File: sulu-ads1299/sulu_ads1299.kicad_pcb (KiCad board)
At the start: 2 copper layers, 42.7 x 64.6 mm, 82 parts, among them J1 73391-0060, J10 through_hole, J11 through_hole, J12 through_hole, J13 through_hole, J14 through_hole, J15 through_hole, J16 through_hole, J17 through_hole, J18 through_hole, J19 through_hole, J2 Conn_01x02, J20 through_hole, J21 through_hole, J22 through_hole, J23 through_hole, J24 through_hole, J25 through_hole, J3 Conn_01x10, J4 Conn_02x10_Odd_Even, J5 Conn_02x11_Odd_Even, J6 Conn_01x02, J7 Conn_02x07_Odd_Even, J8 through_hole, J9 through_hole, SW1 SW_Push, U1 S-85S1AB18-I6T1U, U2 S-85S1AB11-I6T1U, U3 LM2775DSG, U4 ADS1299_TQFP-64, U5 scum3

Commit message: Sulu-ADS1299 started revision 2, added Molex libs, Banana for scale
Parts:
- removed J4: Conn_02x10_Odd_Even, Connector_PinSocket_2.54mm:PinSocket_2x10_P2.54mm_Vertical
- removed J5: Conn_02x11_Odd_Even, Connector_PinSocket_2.54mm:PinSocket_2x11_P2.54mm_Vertical
- removed J7: Conn_02x07_Odd_Even, Connector_PinHeader_2.54mm:PinHeader_2x07_P2.54mm_Vertical
- removed R15: 0 Ohm, Resistor_SMD:R_0402_1005Metric
- removed R3: 42.2K, Resistor_SMD:R_0402_1005Metric
- removed R4: 66.5K, Resistor_SMD:R_0402_1005Metric
- added G***: LOGO, Banana:Banana, F.Cu at (69.8, 54.4)
- added TP1: TestPoint, SCUM:through_hole, F.Cu at (151.3, 72.5)
- added TP10: TestPoint, SCUM:through_hole, F.Cu at (165.6, 59.7)
- added TP11: TestPoint, SCUM:through_hole, F.Cu at (153.1, 72.5)
- added TP12: TestPoint, SCUM:through_hole, F.Cu at (150.8, 74.4)
- added TP13: TestPoint, SCUM:through_hole, F.Cu at (145.0, 80.0)
- added TP14: TestPoint, SCUM:through_hole, F.Cu at (154.3, 69.8)
- added TP15: TestPoint, SCUM:through_hole, F.Cu at (146.2, 74.1)
- added TP16: TestPoint, SCUM:through_hole, F.Cu at (143.3, 80.0)
- added TP2: TestPoint, SCUM:through_hole, F.Cu at (158.6, 66.1)
- added TP3: TestPoint, SCUM:through_hole, F.Cu at (146.2, 78.0)
- added TP4: TestPoint, SCUM:through_hole, F.Cu at (163.8, 59.7)
- added TP5: TestPoint, SCUM:through_hole, F.Cu at (163.3, 61.7)
- added TP6: TestPoint, SCUM:through_hole, F.Cu at (149.1, 76.2)
- added TP7: TestPoint, SCUM:through_hole, F.Cu at (149.1, 74.4)
- added TP8: TestPoint, SCUM:through_hole, F.Cu at (166.8, 57.7)
- added TP9: TestPoint, SCUM:through_hole, F.Cu at (155.7, 68.1)
- C6: value 2.2 uF -> 10 uF
- C_1.8_IN1: value 10 uF -> 4.7 uF
- C_1.8_OUT1: value 10 uF -> 22 uF
- J2: value Conn_01x02 -> Conn_02x05_Odd_Even; footprint Connector_PinHeader_2.54mm:PinHeader_1x02_P2.54mm_Vertical -> Connector_PinSocket_2.54mm:PinSocket_2x05_P2.54mm_Vertical_SMD
- J3: value Conn_01x10 -> Conn_01x08; footprint Connector_PinSocket_2.54mm:PinSocket_1x10_P2.54mm_Vertical -> Molex Connectors:Molex_PicoBlade_53047-0810_1x08_P1.25mm_Vertical; moved to F.Cu
- L1: value 2.2 uH -> 4.7 uH
- SW1: value SW_Push -> SW_DIP_x02; footprint Button_Switch_THT:SW_PUSH_6mm -> Button_Switch_SMD:SW_DIP_SPSTx02_Slide_6.7x6.64mm_W6.73mm_P2.54mm_LowProfile_JPin
- U1: value S-85S1AB18-I6T1U -> TPS62222DDCT; footprint downloaded_libs:SOFL50P180X50-6N -> Package_TO_SOT_SMD:SOT-23-5
- moved J24 110.1 mm to (194.1, 55.8)
- moved J16 108.0 mm to (192.9, 57.7)
- moved J25 107.9 mm to (194.7, 57.5)
- moved C18 105.5 mm to (188.8, 85.6), turned to 0 degrees
- moved C8 105.5 mm to (188.8, 79.7), turned to 0 degrees
- moved C25 105.1 mm to (188.8, 57.9), turned to 0 degrees
- moved J13 103.2 mm to (191.8, 59.5)
- moved C10 101.3 mm to (191.7, 81.7), turned to 0 degrees
- moved C17 98.1 mm to (181.8, 92.1), turned to 0 degrees
- moved J11 98.1 mm to (191.8, 61.3)
- moved J9 97.1 mm to (188.3, 59.7)
- moved J14 96.8 mm to (183.2, 70.1)
- moved J8 95.9 mm to (194.0, 77.6)
- moved J23 95.5 mm to (181.5, 70.1)
- moved C9 92.6 mm to (178.9, 94.0), turned to 0 degrees
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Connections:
- C10 pad 1: /SCUM_GPIO7 -> +1.8V_REG
- C11 pad 1: /SCUM_GPIO7 -> +1.8V_REG
- C21 pad 1: +VDDD -> +1.1V_REG
- C22 pad 1: +VDDD -> +1.1V_REG
- J2 pad 1: /~{ADS_PWDN} -> /ADS_IN1P_CONN
- J2 pad 2: GND -> /ADS_IN1N_CONN
- J3 pad 2: +NRF_VDDD -> /HARD_RESET
- J3 pad 3: +NRF_GND -> /3WB_DATA
- J3 pad 4: /HARD_RESET -> /3WB_ENB
- J3 pad 5: /3WB_DATA -> /3WB_CLK
- J3 pad 6: /3WB_ENB -> /RsRx
- J3 pad 7: GND -> /RsTx
- J3 pad 8: /3WB_CLK -> GND
- R1 pad 1: /SCUM_GPIO7 -> +1.8V_REG
- R2 pad 1: /SCUM_GPIO7 -> +1.8V_REG
- R5 pad 1: +VDDD -> +1.1V_REG
- SW1 pad 2: GND -> /~{ADS_PWDN}
- U1 pad 1: +1.8V_REG -> +EXT_BAT
- U1 pad 3: Net-(L1-Pad2) -> +EXT_BAT
- U1 pad 4: GND -> +1.8V_REG
- U1 pad 5: +EXT_BAT -> Net-(L1-Pad2)
- U4 pad 48: /SCUM_GPIO7 -> +1.8V_REG
- U4 pad 50: /SCUM_GPIO7 -> +1.8V_REG
- U4 pad 52: /SCUM_GPIO7 -> +1.8V_REG
- U5 pad 36: +VDDIO -> +1.8V_REG
- U5 pad 4: +VBAT -> +1.8V_REG
- U5 pad 61: /BOOT_SOURCE_SEL -> +1.1V_REG
- U5 pad 62: +VBAT -> +1.8V_REG
- U5 pad 72: +VDDD -> +1.1V_REG
- U5 pad 90: +VDDD -> +1.1V_REG
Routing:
- net +EXT_BAT: track 82.7 -> 0.00 mm, vias 4 -> 0
- net +5V_REG: track 79.1 -> 0.00 mm, vias 4 -> 0
- net /SCUM_GPIO7: track 59.4 -> 0.00 mm, vias 1 -> 0
- net +VBAT: track 58.1 -> 0.00 mm, vias 2 -> 0
- net +VDDIO: track 45.7 -> 0.00 mm, vias 2 -> 0
- net GND: track 44.6 -> 0.00 mm, vias 1 -> 0
- net /~{ADS_RESET}: track 38.8 -> 0.00 mm
- net +VDDD: track 38.0 -> 0.00 mm
- net /ADS_GPIO3: track 35.2 -> 0.00 mm, vias 1 -> 0
- net /ADS_GPIO4: track 34.0 -> 0.00 mm, vias 1 -> 0
- net /ADS_GPIO1: track 30.7 -> 0.00 mm, vias 1 -> 0
- net /ADS_GPIO2: track 29.9 -> 0.00 mm, vias 1 -> 0
- net /SENSOR_LDO_OUTPUT: track 26.9 -> 0.00 mm, vias 1 -> 0
- net /SCUM_GPIO14: track 21.8 -> 0.00 mm, vias 1 -> 0
- net /BOOT_SOURCE_SEL: track 21.4 -> 0.00 mm, vias 1 -> 0
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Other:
- board size 42.7 x 64.6 mm -> 42.7 x 35.4 mm
- board text removed: "+"
- board text removed: "-"
- board text removed: "0"
- board text removed: "1"
- board text removed: "10"
- board text removed: "11"
- board text removed: "12"
- board text removed: "13"
- board text removed: "14"
- board text removed: "15"
- board text removed: "2"
- board text removed: "3"
- board text removed: "3WB CLK"
- board text removed: "3WB DATA"
- board text removed: "3WB ENB"
- board text removed: "4"
- board text removed: "5"
- board text removed: "6"
- board text removed: "7"
- board text removed: "8"
- board text removed: "9"
- board text removed: "ADC IN"
- board text removed: "ADS_PWDN"
- board text removed: "ADS_RESET"
- board text removed: "GPIO"
- board text removed: "GPIO1"
- board text removed: "GPIO2"
- board text removed: "GPIO3"
- board text removed: "GPIO4"
- board text removed: "HARD RESET"
- board text removed: "IN1+"
- board text removed: "IN1-"
- board text removed: "IN2+"
- board text removed: "IN2-"
- board text removed: "IN3+"
- board text removed: "IN3-"
- board text removed: "IN4+"
- board text removed: "IN4-"
- board text removed: "NRF GND"
- board text removed: "NRF VDDD"
- board text removed: "RsRx"
- board text removed: "RsTx"
- board text removed: "VBAT"
- board text removed: "VDDD"

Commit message: Updated sulu-ads1299 rev2 layout and schematic
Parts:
- removed J1: 73391-0060, downloaded_libs:MOLEX_73391-0060
- moved C8 77.3 mm to (111.6, 76.6), turned to 90 degrees
- moved C7 76.1 mm to (87.6, 76.0), turned to 90 degrees
- moved C6 73.5 mm to (93.1, 75.7)
- moved C5 69.4 mm to (98.0, 52.8), turned to 180 degrees
- moved R7 68.7 mm to (98.6, 83.3), turned to 90 degrees
- moved C20 67.5 mm to (111.1, 71.6), turned to 90 degrees
- moved C30 64.3 mm to (101.1, 81.8)
- moved R1 59.3 mm to (111.4, 82.3)
- moved C_1.8_OUT1 50.8 mm to (93.1, 74.7), turned to 180 degrees
- moved R2 45.3 mm to (111.4, 83.3)
- moved R10 43.1 mm to (101.6, 83.3), turned to 90 degrees
- moved R14 42.0 mm to (105.7, 83.3), turned to 90 degrees
- moved C27 40.9 mm to (103.1, 81.8)
- moved R9 40.8 mm to (100.6, 83.3), turned to 90 degrees
- moved R8 38.7 mm to (99.6, 83.3), turned to 90 degrees
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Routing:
- net /3WB_ENB: track 0.00 -> 9.21 mm, vias 0 -> 2
- net /3WB_DATA: track 0.00 -> 7.89 mm, vias 0 -> 2
- net /SCUM_GPIO12: track 0.00 -> 6.94 mm, vias 0 -> 2
- net /SCUM_GPIO13: track 0.00 -> 3.26 mm
- net /SCUM_GPIO14: track 0.00 -> 2.81 mm
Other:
- board size 42.7 x 35.4 mm -> 32.4 x 42.7 mm

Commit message: Sulu-ADS1299 rev2 component placements
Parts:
- moved C25 98.1 mm to (90.9, 64.4)
- moved C24 85.9 mm to (92.2, 61.1), turned to 90 degrees
- moved C22 83.3 mm to (91.3, 67.7)
- moved R6 81.0 mm to (107.8, 57.1), turned to -90 degrees
- moved C16 78.2 mm to (111.0, 73.9)
- moved R5 76.6 mm to (99.9, 52.7)
- moved J12 75.8 mm to (112.6, 68.1)
- moved C2 8.13 mm to (139.6, 80.0)
- moved C5 0.13 mm to (98.0, 52.7)
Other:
- outline, holes or cut-outs redrawn

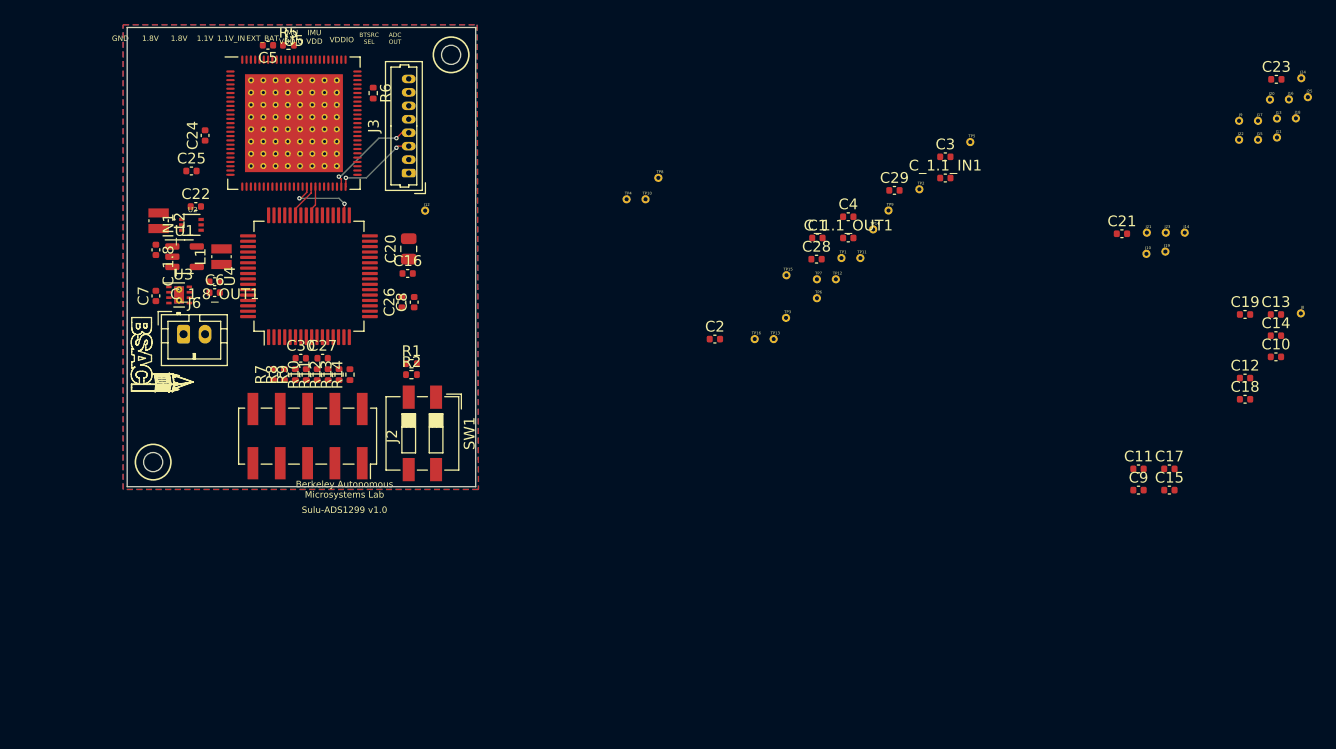
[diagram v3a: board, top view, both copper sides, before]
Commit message: Sulu-ADS1299 components placed, new antenna, some routing
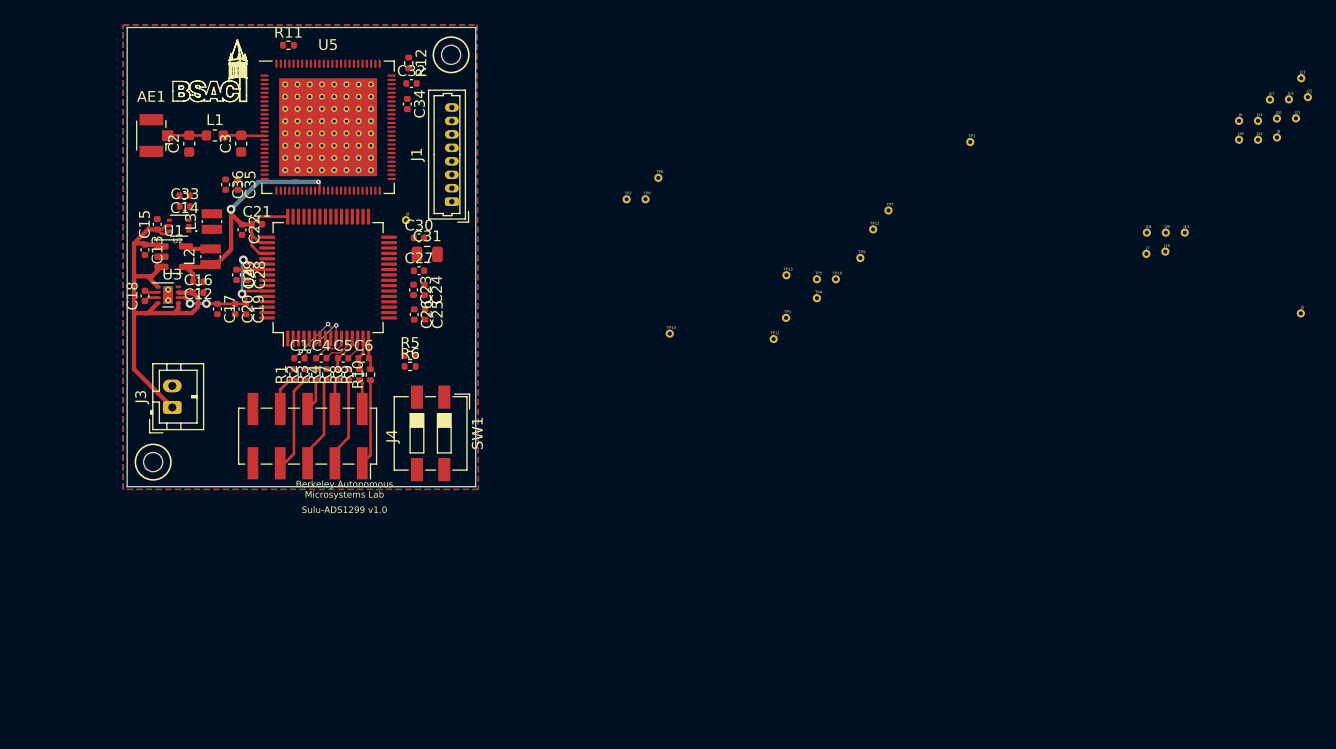
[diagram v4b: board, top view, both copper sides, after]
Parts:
- removed the C1 at (149.1, 70.6)
- removed the C4 at (152.0, 68.6)
- removed the C5 at (98.0, 52.7)
- removed G***: LOGO, Banana:Banana
- removed the TP1 at (151.3, 72.5)
- removed the TP2 at (158.6, 66.1)
- added AE1: FXP70.07.0053A, Connector_Coaxial:U.FL_Hirose_U.FL-R-SMT-1_Vertical, F.Cu at (87.7, 61.1)
- added L1: 2.2 uH, Inductor_SMD:L_0603_1608Metric, F.Cu at (93.1, 61.1)
- C2, C3: value NP -> 22 uF; footprint Capacitor_SMD:C_0402_1005Metric -> Capacitor_SMD:C_0603_1608Metric
- moved C21 95.5 mm to (97.0, 69.3)
- moved C29 94.4 mm to (95.1, 74.0), turned to -90 degrees
- moved C28 87.5 mm to (96.1, 74.0), turned to -90 degrees
- moved C22 86.2 mm to (95.6, 69.8), turned to -90 degrees
- moved C20 85.6 mm to (95.0, 77.2), turned to -90 degrees
- moved C34 80.8 mm to (111.0, 58.2), turned to -90 degrees
- moved C24 79.2 mm to (112.6, 75.4), turned to -90 degrees
- moved C25 79.1 mm to (112.6, 77.7), turned to -90 degrees
- moved C23 77.7 mm to (111.6, 75.4), turned to -90 degrees
- moved C30 77.1 mm to (112.1, 70.6)
- moved C15 73.4 mm to (87.8, 69.3), turned to 90 degrees
- moved C26 72.0 mm to (111.6, 77.7), turned to -90 degrees
- moved C32 67.5 mm to (111.4, 56.3)
- moved C3 65.4 mm to (95.6, 61.8), turned to 90 degrees
- moved C14 61.8 mm to (90.3, 66.7), turned to 180 degrees
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- renumbered C29 to C1, C_1.8_OUT1 to C12, C_1.8_IN1 to C13, C_1.1_OUT1 to C14, C_1.1_IN1 to C15, C6 to C16, C26 to C17, C7 to C18, C8 to C19, C9 to C20, C10 to C21, C11 to C22, C12 to C23, C13 to C24, C14 to C25, C15 to C26, C16 to C27, C17 to C28, C18 to C29, C19 to C30, C20 to C31, C21 to C32, C22 to C33, C23 to C34, C24 to C35, C25 to C36, C30 to C4, C27 to C5, C28 to C6, J3 to J1, J13 to J10, J14 to J11, J15 to J12, J16 to J13, J17 to J14, J18 to J15, J19 to J16, J20 to J17, J21 to J18, J22 to J19, J23 to J20, J24 to J21, J25 to J22, J6 to J3, J2 to J4, J8 to J5, J9 to J6, J10 to J7, J11 to J8, J12 to J9, L1 to L2, L2 to L3, R7 to R1, R14 to R10, R5 to R11, R6 to R12, R8 to R2, R9 to R3, R10 to R4, R1 to R5, R2 to R6, R11 to R7, R12 to R8, R13 to R9, TP3 to TP1, TP12 to TP10, TP13 to TP11, TP14 to TP12, TP15 to TP13, TP16 to TP14, TP4 to TP2, TP5 to TP3, TP6 to TP4, TP7 to TP5, TP8 to TP6, TP9 to TP7, TP10 to TP8, TP11 to TP9
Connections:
- C15 pad 1: /1.1V_IN -> +EXT_BAT
- C2 pad 1: +VBAT -> GND
- C2 pad 2: GND -> Net-(AE1-Pad1)
- C3 pad 1: +VDDIO -> GND
- C3 pad 2: GND -> /SCuM-3C/ANTENNA
- J1 pad 1: +VBAT -> +EXT_BAT
- U2 pad 5: /1.1V_IN -> +EXT_BAT
- U2 pad 6: /1.1V_IN -> +EXT_BAT
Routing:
- net +EXT_BAT: track 0.00 -> 40.8 mm
- net +1.8V_REG: track 0.00 -> 32.8 mm, vias 0 -> 2
- net +5V_REG: track 0.00 -> 15.7 mm, vias 0 -> 4
- net /3WB_ENB: track 9.21 -> 0.00 mm, vias 2 -> 0
- net /ADS_IN4P_CONN: track 0.00 -> 8.91 mm
- net /ADS_IN3P_CONN: track 0.00 -> 8.46 mm
- net /ADS_IN2P_CONN: track 0.00 -> 8.25 mm
- net /ADS_IN1P_CONN: track 0.00 -> 8.04 mm
- net /3WB_DATA: track 7.89 -> 0.00 mm, vias 2 -> 0
- net /SCUM_GPIO12: track 6.94 -> 0.00 mm, vias 2 -> 0
- net /ADS_IN4N: track 0.00 -> 5.93 mm, vias 0 -> 2
- net /ADS_IN4P: track 0.00 -> 5.57 mm, vias 0 -> 2
- net /SCuM-3C/ANTENNA: track 0.00 -> 3.85 mm
- net Net-(AE1-Pad1): track 0.00 -> 3.61 mm
- net /ADS_IN3N: track 0.00 -> 3.48 mm
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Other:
- board text removed: "1.1V"
- board text removed: "1.1V_IN"
- board text removed: "1.8V"
- board text removed: "ADC OUT"
- board text removed: "BTSRC SEL"
- board text removed: "EXT_BAT"
- board text removed: "GND"
- board text removed: "IMU VDD"
- board text removed: "IMU VDDIO"
- board text removed: "VDDIO"

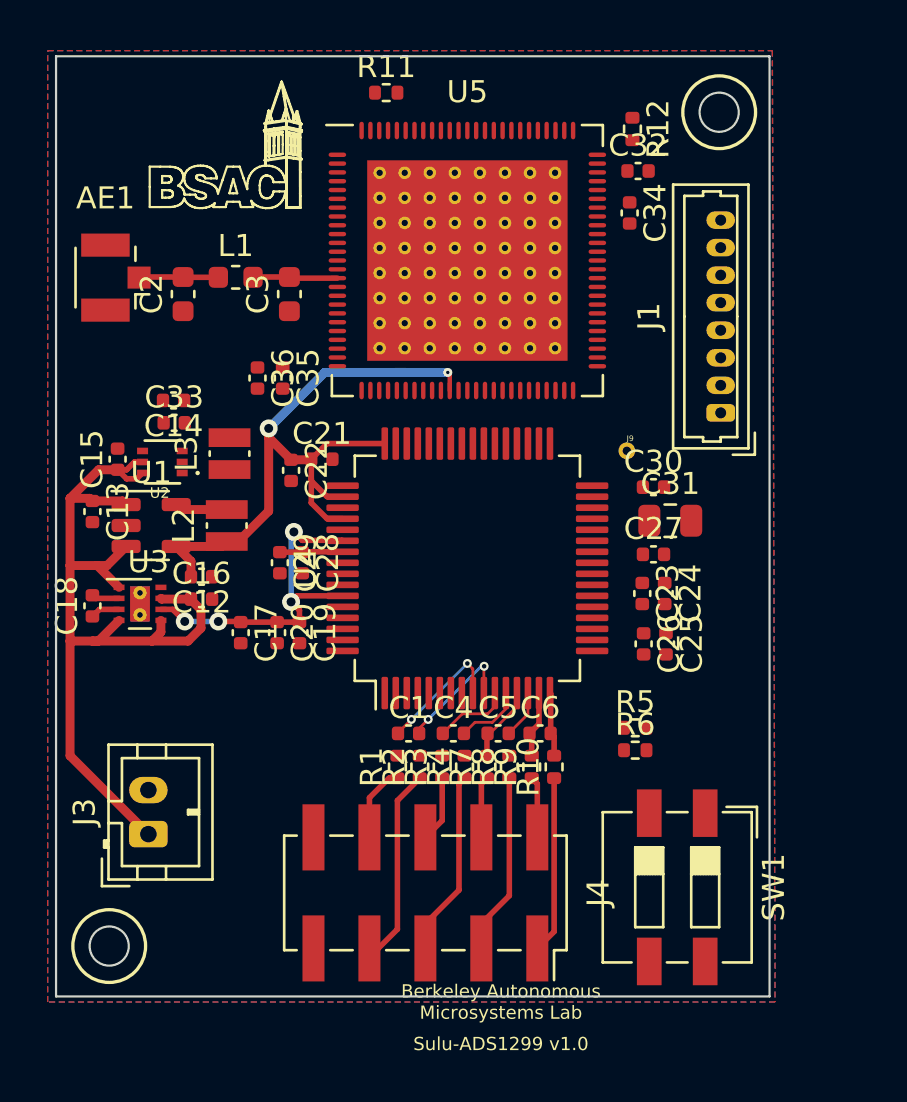
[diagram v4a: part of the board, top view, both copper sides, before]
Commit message: Sulu-ADS1299 rev2 most of the routing done
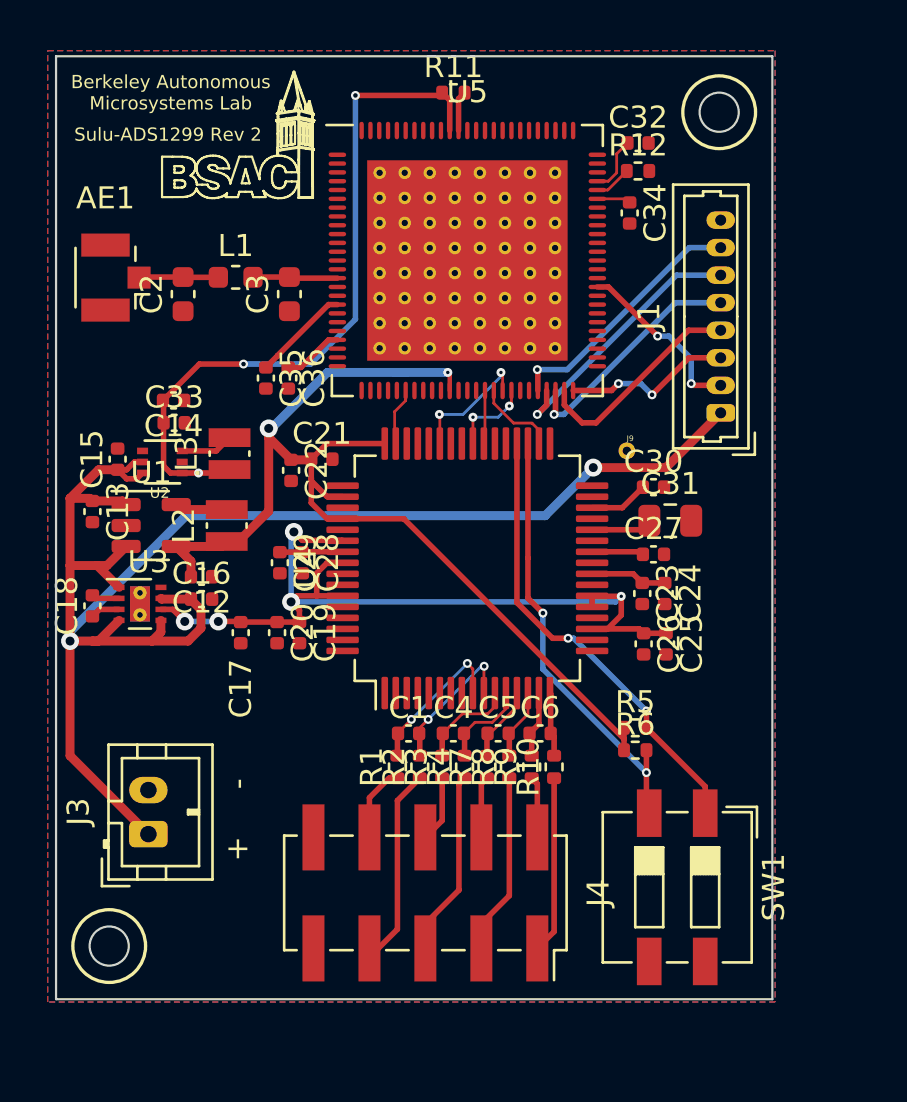
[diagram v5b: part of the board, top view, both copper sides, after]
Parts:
- moved R11 3.05 mm to (103.0, 52.7)
- moved R12 1.92 mm to (111.4, 56.3), turned to 0 degrees
- moved C36 1.40 mm to (95.5, 65.7)
- moved C32 1.27 mm to (111.4, 55.0)
- moved C35 0.76 mm to (94.5, 65.7)
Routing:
- net +1.1V_REG: track 0.00 -> 35.0 mm, vias 0 -> 3
- net +EXT_BAT: track 40.8 -> 74.9 mm, vias 0 -> 2
- net +5V_REG: track 15.7 -> 40.9 mm, vias 4 -> 5
- net /~{ADS_RESET}: track 0.00 -> 20.9 mm, vias 0 -> 2
- net /~{ADS_PWDN}: track 0.00 -> 20.1 mm, vias 0 -> 2
- net +1.8V_REG: track 32.8 -> 50.7 mm
- net /RsRx: track 0.00 -> 12.2 mm, vias 0 -> 1
- net /RsTx: track 0.00 -> 11.6 mm, vias 0 -> 1
- net /3WB_CLK: track 0.00 -> 10.8 mm, vias 0 -> 1
- net /3WB_ENB: track 0.00 -> 9.83 mm
- net /HARD_RESET: track 0.00 -> 8.12 mm, vias 0 -> 2
- net /3WB_DATA: track 0.00 -> 7.73 mm, vias 0 -> 2
- net /SCUM_GPIO13: track 0.00 -> 5.87 mm, vias 0 -> 2
- net Net-(C35-Pad1): track 0.00 -> 4.43 mm
- net /SCUM_GPIO14: track 0.00 -> 3.80 mm, vias 0 -> 2
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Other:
- board size 32.4 x 42.7 mm -> 32.5 x 42.8 mm
- board text added: "+"
- board text added: "-"
- board text added: "Sulu-ADS1299 Rev 2"
- board text removed: "Sulu-ADS1299 v1.0"
